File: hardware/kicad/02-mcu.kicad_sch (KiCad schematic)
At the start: 6 parts, among them U1 ESP32-S3-N16R8

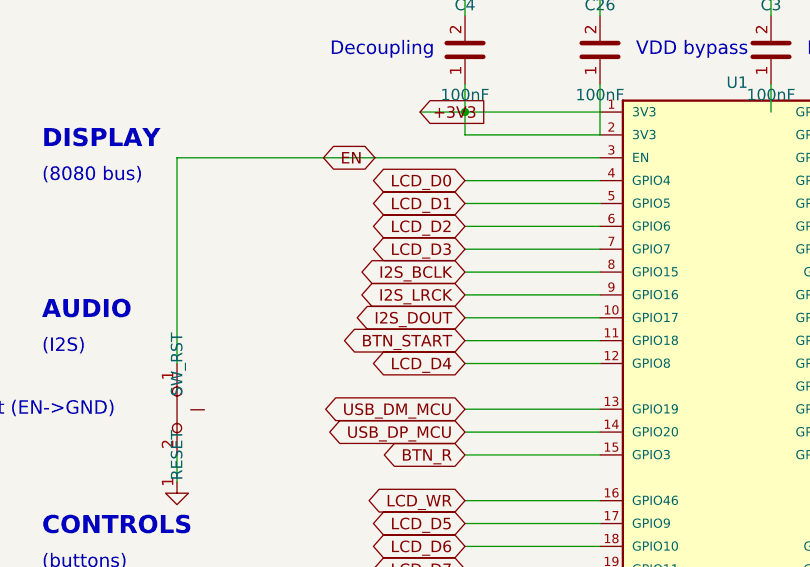
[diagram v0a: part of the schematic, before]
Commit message: R10-LOW-2: retire the I2S_BCLK/I2S_LRCK reservation nets — 28-file chain, one commit
The two nets had exactly one pin each (U1.8, U1.9) and zero copper, kept
alive since R10 by the claim "reserved for historical reasons" — while
production audio.c runs PDM TX with .clk = I2S_GPIO_UNUSED and drives only
DOUT. A net name with one pin is a label, not a circuit, and keeping the
label cost three gate allowlists and one lie: the generated TEST firmware
passed .clk = I2S_BCLK (GPIO15), disagreeing with the production firmware
about a pin adjacent to the strapping set.

Generators: config.py drops GPIO15/16 from GPIO_NETS (mcu.py's fallback
labels them plain GPIO15/GPIO16, same as the PSRAM trio) and AUDIO_NETS is
["I2S_DOUT"]; primitives.NET_LIST gap-retires ids 24/25 like 18/19;
routing/audio.py stops injecting the pad nets; datasheet_specs U1 pins 8/9
become _unconnected() with the retirement dated in the function text.

Gates — three allowlists DIE rather than grow:
  verify_design_intent  KNOWN_SINGLE is EMPTY (its last two tenants gone),
                        DIRECT_ROUTED deleted — its own comment was false
                        twice over ("directly routed" nets with no copper,
                        an info() telling the reader to verify a trace that
                        does not exist), and T14 now asserts the nets STAY
                        retired: reappearing is the regression.
  drc_check             _UNROUTED_OK is empty — every unrouted net is a
                        finding again.
  verify_netlist_diff   GPIO15/16 join T1_ALLOW beside the PSRAM pins, with
                        the evidence in the comment.
  verify_ground_loops / verify_signal_chain_complete / verify_test_points /
  verify_polarity / pcb_review updated; polarity's stale "pins 8/9 get net
  0" comment (they had nets 24/25) corrected to match reality.

Firmware: generate_hw_tests.py emits .clk = I2S_GPIO_UNUSED matching
production, and reads only I2S_DOUT from board_config.h; tes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
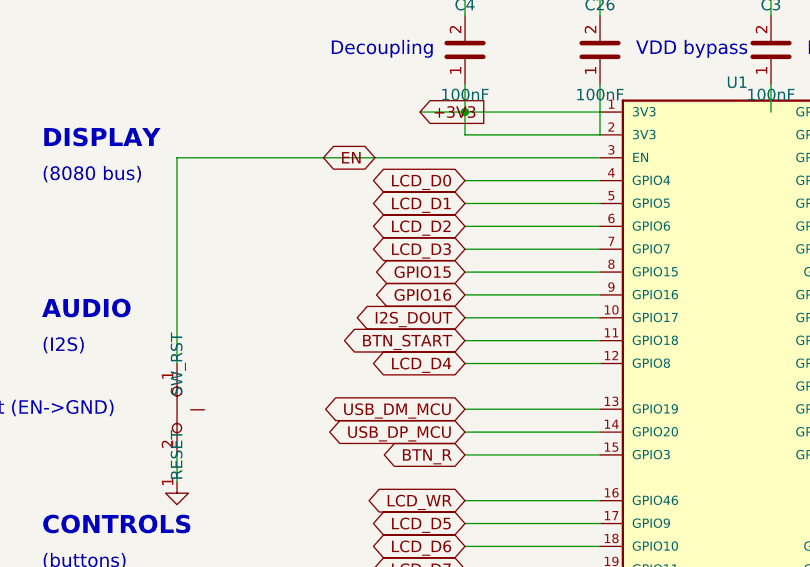
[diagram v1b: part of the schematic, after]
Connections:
- net I2S_BCLK renamed GPIO15
- net I2S_LRCK renamed GPIO16
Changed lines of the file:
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@@
   (global_label "LCD_D3" (shape bidirectional) (at 169.76 147.14 180) (effects (font (size 1.27 1.27))) (property "Intersheetrefs" "" (at 0 0 0) (effects (font (size 1.27 1.27)) hide)))
   (wire (pts (xy 184.76 149.68) (xy 169.76 149.68)) (stroke (width 0) (type default)))
-  (global_label "I2S_BCLK" (shape bidirectional) (at 169.76 149.68 180) (effects (font (size 1.27 1.27))) (property "Intersheetrefs" "" (at 0 0 0) (effects (font (size 1.27 1.27)) hide)))
+  (global_label "GPIO15" (shape bidirectional) (at 169.76 149.68 180) (effects (font (size 1.27 1.27))) (property "Intersheetrefs" "" (at 0 0 0) (effects (font (size 1.27 1.27)) hide)))
   (wire (pts (xy 184.76 152.22) (xy 169.76 152.22)) (stroke (width 0) (type default)))
-  (global_label "I2S_LRCK" (shape bidirectional) (at 169.76 152.22 180) (effects (font (size 1.27 1.27))) (property "Intersheetrefs" "" (at 0 0 0) (effects (font (size 1.27 1.27)) hide)))
+  (global_label "GPIO16" (shape bidirectional) (at 169.76 152.22 180) (effects (font (size 1.27 1.27))) (property "Intersheetrefs" "" (at 0 0 0) (effects (font (size 1.27 1.27)) hide)))
   (wire (pts (xy 184.76 154.76) (xy 169.76 154.76)) (stroke (width 0) (type default)))
   (global_label "I2S_DOUT" (shape bidirectional) (at 169.76 154.76 180) (effects (font (size 1.27 1.27))) (property "Intersheetrefs" "" (at 0 0 0) (effects (font (size 1.27 1.27)) hide)))

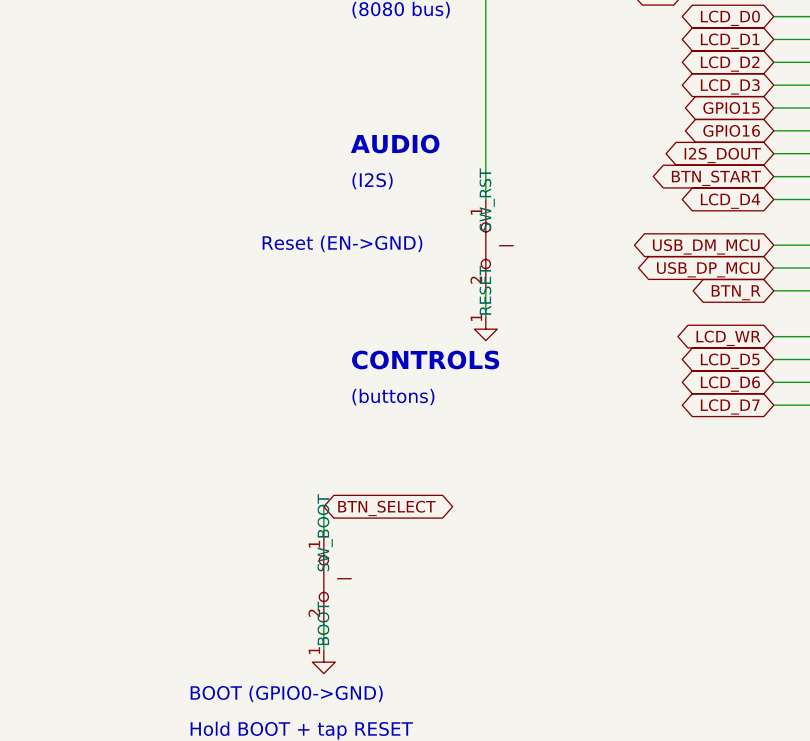
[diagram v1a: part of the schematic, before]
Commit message: refactor(refs): rename SW_PWR/SW_BOOT/SW_RST to IPC SW16/SW14/SW15
KiBot (>= 1.6.5, upstream #604, wontfix) hard-rejects schematic
references that are not PREFIX+NUMBER, which blocked its schematic
phase (ERC + BOM cross-check) forever. User-approved rename across the
whole chain in one commit: generators (PCB + schematics), datasheet
specs, verify scripts, vbench (scenarios, netlist, sim headers), skills,
issues, docs, website — plus regenerated .kicad_pcb/.kicad_sch, BOM,
CPL, d356, gerbers, renders, iBOM, Net Explorer, and release_jlcpcb/
fully synced. SW13 was already the MENU button, so the switches take
SW14 (BOOT), SW15 (RST), SW16 (PWR slide). Both datasheet PDFs
(hardware/datasheets/ + website/static/datasheets/) renamed to match.

external-dfm.sh: single full KiBot run restored (-e included) with a
regression guard on "Malformed component reference"; CI workflow
extended the same way. Three latent script bugs fixed while unblocking
paths that had never executed: bare failing python under set -e killed
the script before the summary; grep|head SIGPIPE (141) under pipefail;
and the ERC JSON parser read top-level violations[] (the DRC shape)
while ERC nests them under sheets[] — a false "0 errors". KiBot BOM
CSV parsing now handles KiBot 1.9's space-separated refs + stats block.

First-ever ERC run found 4 error-level schematic-DRAWING bugs (dangling
GND in controls, dangling BTN_LEFT label in mcu, +3V3 with no power
driver x2) — pre-existing, copper unaffected, recorded in memory as
owned follow-up work for generate_schematics. make external-dfm is red
on them honestly.

Tests: verify-all 77/77, gate-coverage 9/9 fault classes caught,
verify-fast 124/124, verify-dfa 9/9, firmware-sync-check PASS,
KiBot DRC 0 errors, BOM cross-ref 81/81 assembled parts matched,
website-build green.

Co-Authored-By: Claude Fable 5 <noreply@anthropic.com>
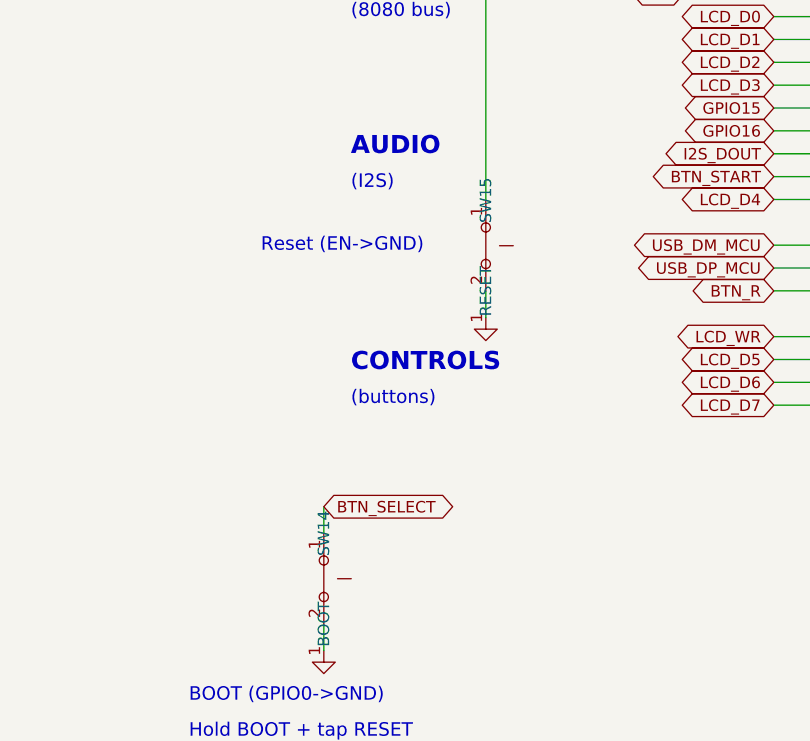
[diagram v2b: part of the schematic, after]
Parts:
- renumbered SW_BOOT to SW14, SW_RST to SW15
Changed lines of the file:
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@@
   (text "EN bare on v1 — R3 DNP, no RC" (at 137.76 113 0) (effects (font (size 1.5 1.5)) (justify left)))
   (text "v2: 10k + 100nF at pin 3" (at 137.76 117 0) (effects (font (size 1.5 1.5)) (justify left)))
-  (symbol (lib_id "SW_Push") (at 137.76 164.98 270) (unit 1) (exclude_from_sim no) (in_bom yes) (on_board yes) (dnp no) (property "Reference" "SW_RST" (at 137.76 159.932 0) (effects (font (size 1.27 1.27)))) (property "Value" "RESET" (at 137.76 170.028 0) (effects (font (size 1.27 1.27)))) (pin "1") (pin "2") (instances (project "esp32-emu-turbo" (path "/00000003-cafe-4000-8000-000000000003" (reference "SW_RST") (unit 1)))))
+  (symbol (lib_id "SW_Push") (at 137.76 164.98 270) (unit 1) (exclude_from_sim no) (in_bom yes) (on_board yes) (dnp no) (property "Reference" "SW15" (at 137.76 159.932 0) (effects (font (size 1.27 1.27)))) (property "Value" "RESET" (at 137.76 170.028 0) (effects (font (size 1.27 1.27)))) (pin "1") (pin "2") (instances (project "esp32-emu-turbo" (path "/00000003-cafe-4000-8000-000000000003" (reference "SW15") (unit 1)))))
   (wire (pts (xy 137.76 159.89999999999998) (xy 137.76 136.98)) (stroke (width 0) (type default)))
   (wire (pts (xy 159.76 136.98) (xy 137.76 136.98)) (stroke (width 0) (type default)))
@@
   (wire (pts (xy 137.76 170.06) (xy 137.76 172.98)) (stroke (width 0) (type default)))
   (text "Reset (EN->GND)" (at 112.75999999999999 164.98 0) (effects (font (size 1.5 1.5)) (justify left)))
-  (symbol (lib_id "SW_Push") (at 119.75999999999999 201.98 270) (unit 1) (exclude_from_sim no) (in_bom yes) (on_board yes) (dnp no) (property "Reference" "SW_BOOT" (at 119.75999999999999 196.932 0) (effects (font (size 1.27 1.27)))) (property "Value" "BOOT" (at 119.75999999999999 207.028 0) (effects (font (size 1.27 1.27)))) (pin "1") (pin "2") (instances (project "esp32-emu-turbo" (path "/00000003-cafe-4000-8000-000000000003" (reference "SW_BOOT") (unit 1)))))
+  (symbol (lib_id "SW_Push") (at 119.75999999999999 201.98 270) (unit 1) (exclude_from_sim no) (in_bom yes) (on_board yes) (dnp no) (property "Reference" "SW14" (at 119.75999999999999 196.932 0) (effects (font (size 1.27 1.27)))) (property "Value" "BOOT" (at 119.75999999999999 207.028 0) (effects (font (size 1.27 1.27)))) (pin "1") (pin "2") (instances (project "esp32-emu-turbo" (path "/00000003-cafe-4000-8000-000000000003" (reference "SW14") (unit 1)))))
   (global_label "BTN_SELECT" (shape bidirectional) (at 119.75999999999999 193.98 0) (effects (font (size 1.27 1.27))) (property "Intersheetrefs" "" (at 0 0 0) (effects (font (size 1.27 1.27)) hide)))
   (wire (pts (xy 119.75999999999999 196.89999999999998) (xy 119.75999999999999 193.98)) (stroke (width 0) (type default)))

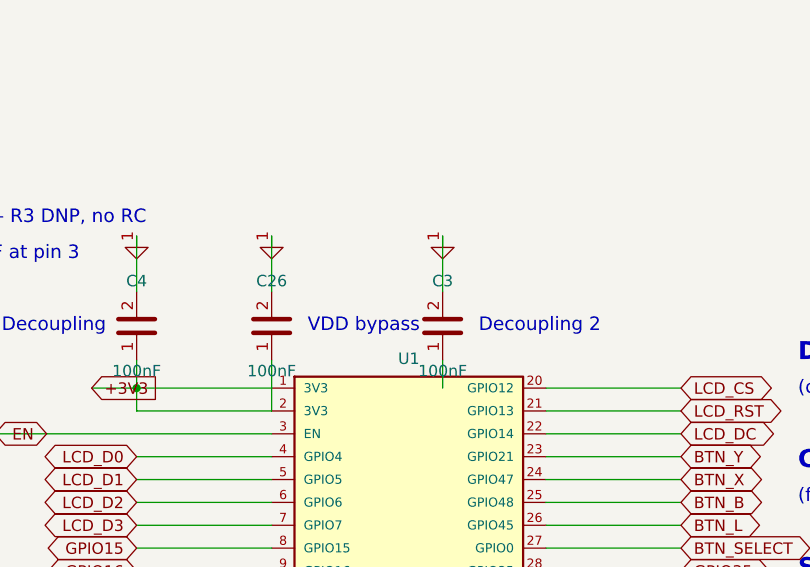
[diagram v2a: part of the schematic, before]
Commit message: fix(schematics): first clean ERC — uuid collisions, instance paths, C3 float
The first-ever ERC run (unlocked by the SW ref rename) reported errors
on geometrically perfect cells while skipping their identical twins.
Root causes, both in generate_schematics:

1. Cross-sheet uuid collisions — every sheet's context counted 1,2,3...
   into the same "{n}-cafe-4000-8000-{n}" pattern, so the same uuid
   lived in several files. ERC merged unrelated objects across sheets:
   phantom "pin not connected" findings, wrong-sheet attribution, and
   pins silently DROPPED from the exported netlist (L1.2/U2.7/Q1.1/
   R24.1 did not exist, which is why netlist-diff T4 "passed"). uuids
   now carry a per-file namespace nibble in the variant group.
2. Single-level symbol instance paths ("/<sheet-uuid>") — loaders fell
   back to "the first instance" (KiBot W182). Both accepted shapes are
   now emitted; KiCad's netlister and ERC resolve different ones.

Real findings fixed once the phantoms cleared:
- C3 (ESP32 decoupling): its +3V3 tap wire ended in the gap between the
  +3V3 wire (ends x=184.76) and the LCD_CS stub (starts x=215.24) —
  floating, one step from a drawn +3V3/LCD_CS short. Moved between C4
  and the module edge, junction added, caption moved off C26.
- SW16 pin 2: explicit no_connect (throw side deliberately unrouted on
  v1 — see project_swpwr memory).
- PWR_FLAG on +3V3 and GND (+5V must NOT get one: IP5306 VOUT is
  power_out). LX and RPP_GATE now labelled with the PCB's net names;
  both closed out of verify_netlist_diff T2_ALLOW — two more nodes the
  cross-check actually verifies.

New standing gate: scripts/verify_erc.py (make verify-erc) — KiCad ERC
at error severity, in VERIFY_ALL_SCRIPTS, routed by the existing `erc`
law (pcb-engineer, dead-board), proven by mutation (deleting C3's
junction turns it red). .claudeheavy covers the new KiBot ERC/DRC JSON
reports and ESP-IDF managed_components.

Not gated on purpose: 651 warning-severity ERC findings (endpoint_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
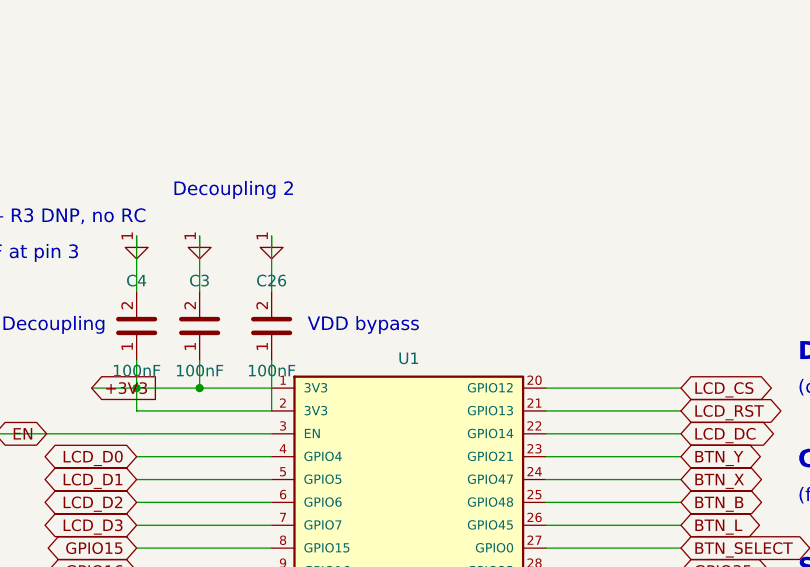
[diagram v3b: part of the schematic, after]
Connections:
- net +3V3: now also C3.1
